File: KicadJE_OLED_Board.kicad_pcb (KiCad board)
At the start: 2 copper layers, 170.6 x 128 mm, 189 parts, among them J1 LED 1-6, J101 Out1, J102 IN1, J103 OUT1, J104 Out1, J105 IN1, J106 OUT1, J201 OLED, J202 ADC Input, J203 Out2, J204 Out1, J205 OUT1, J206 OUT2, J207 IN1, J208 IN2, J209 CV1, J210 CV2, J211 FrontLED, J212 -12V Front, J301 UART, J302 AVR-ISP-6, P1 Doepfer_Power_16pin, P101 Doepfer_Power_10pin, P201 Doepfer_Power_16pin, SW201 Rotary_Encoder_Switch, SW202 Rotary_Encoder_Switch, U101 TL072, U201 TL072, U202 TL072, U301 ATmega32A-AU, Y301 16MHz

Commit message: Update KicadJE_OLED_Board.kicad_pcb
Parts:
- C105, C106, D101, D102, R112: moved to F.Cu
- moved D105 142.4 mm to (125.6, 130.1)
- moved D106 142.4 mm to (125.6, 133.5)
- moved D104 132.4 mm to (133.0, 130.0)
- moved D101 128.5 mm to (144.0, 61.0), turned to 270 degrees
- moved D107 127.5 mm to (133.0, 134.0)
- moved D102 112.9 mm to (144.0, 69.0), turned to 270 degrees
- moved C105 105.6 mm to (154.0, 90.0), turned to 180 degrees
- moved J101 104.8 mm to (147.0, 106.0)
- moved C106 102.3 mm to (148.1, 81.5), turned to 180 degrees
- moved J104 99.0 mm to (153.0, 106.0)
- moved U101 75.2 mm to (151.0, 86.0)
- moved R112 65.6 mm to (155.0, 65.0), turned to 270 degrees
- moved TP101 53.9 mm to (143.0, 45.0)
- moved R109 34.7 mm to (168.0, 34.0)
- moved H101 31.7 mm to (151.0, 47.0)
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
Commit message: Amp/Filt
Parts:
- added J107: In1, Connector_PinSocket_2.54mm:PinSocket_1x02_P2.54mm_Vertical, B.Cu at (148.0, 98.2)
- added J108: InFlt, Connector_PinSocket_2.54mm:PinSocket_1x02_P2.54mm_Vertical, B.Cu at (152.0, 98.2)
- J104: value Out1 -> OutFlt
- J105: value IN1 -> INFLT
- J106: value OUT1 -> OUTFLT
- moved R103 111.2 mm to (148.0, 115.0)
- moved R114 106.7 mm to (148.0, 125.0)
- moved R113 72.1 mm to (101.8, 26.5)
- moved R104 71.3 mm to (107.3, 26.5)
- moved R106 70.7 mm to (112.8, 26.5)
- moved C103 60.3 mm to (102.0, 39.0)
- moved R102 60.3 mm to (108.0, 35.0)
- moved R117 49.5 mm to (118.2, 26.5)
- moved R109 48.9 mm to (136.0, 71.0)
- moved R110 48.8 mm to (123.7, 26.5)
- moved R105 47.5 mm to (129.2, 26.5)
- moved D105 31.2 mm to (151.0, 112.0), turned to 90 degrees
- moved D106 26.2 mm to (151.0, 127.0), turned to 90 degrees
- moved C104 25.0 mm to (134.6, 26.5)
- moved D104 22.2 mm to (151.0, 117.0), turned to 90 degrees
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
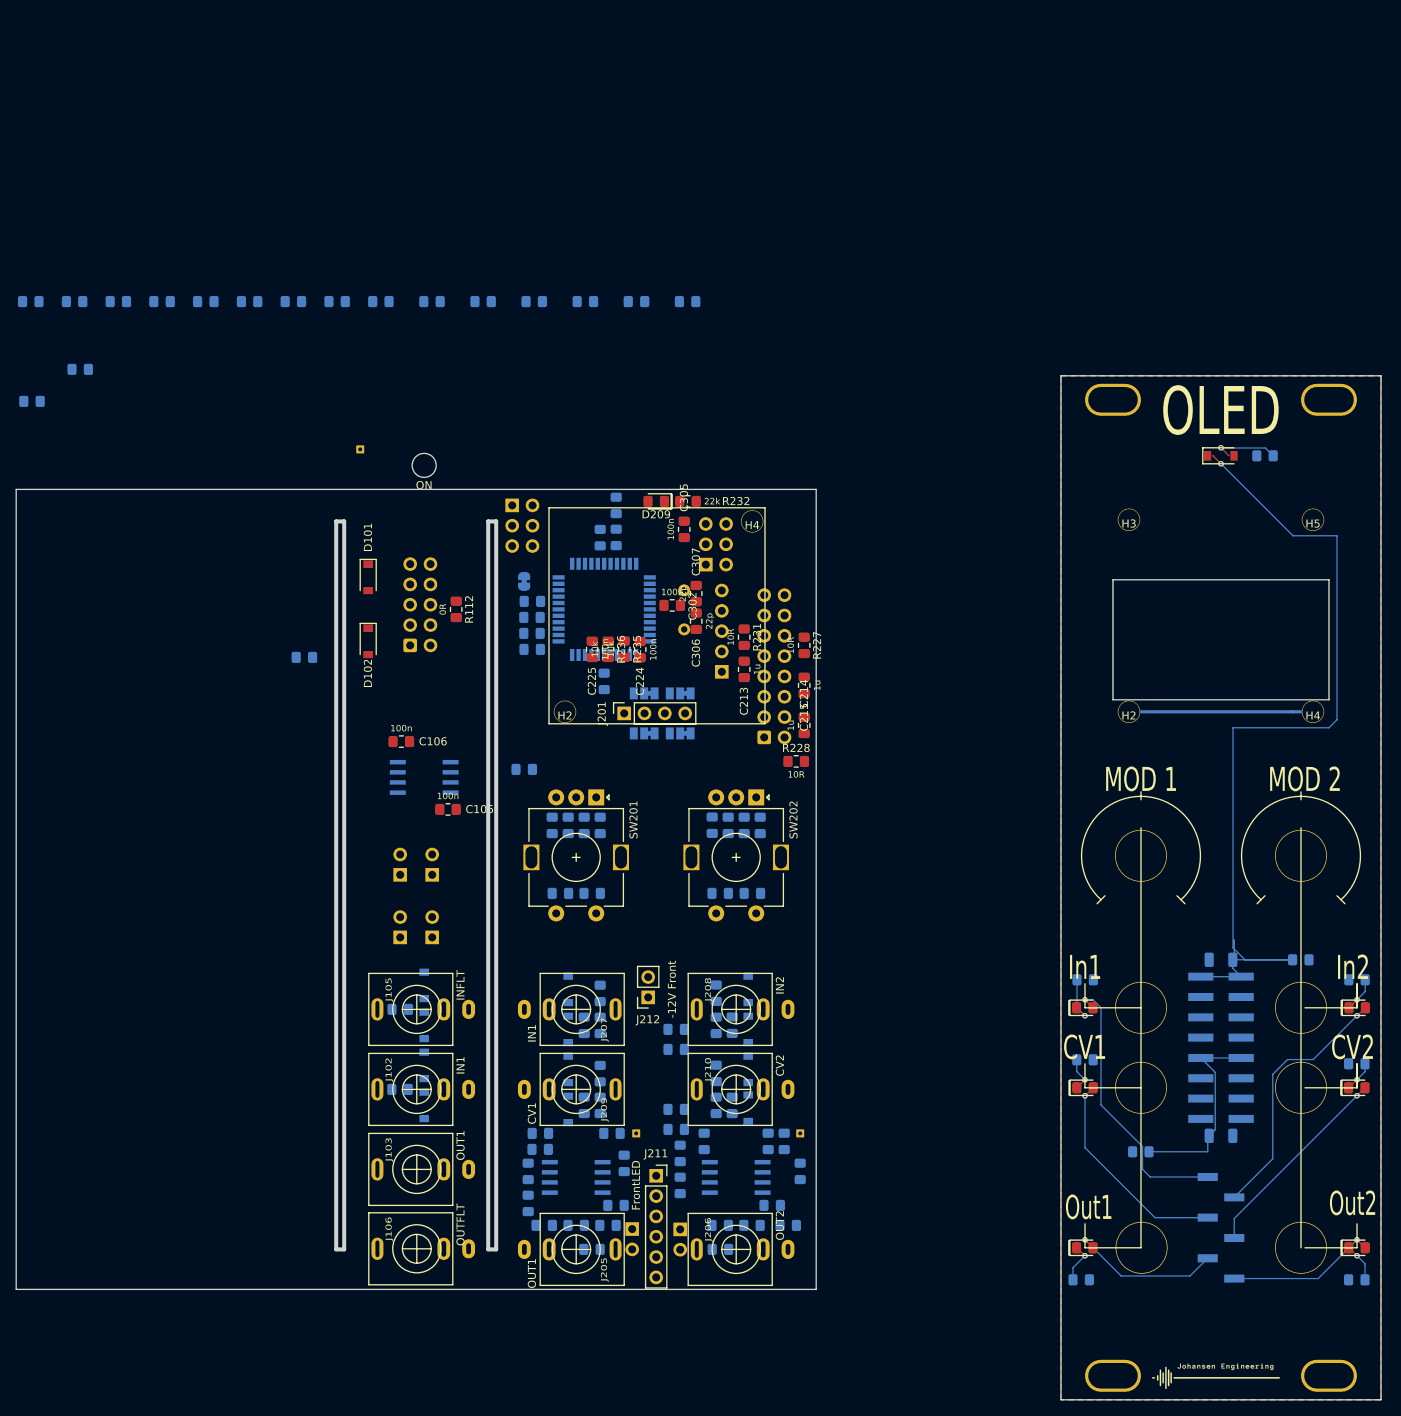
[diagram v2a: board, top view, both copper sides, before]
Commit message: move pinhdr from in jacks to input circuit
after protection resistor - so pcb may be cut above the connectors in case this is needed
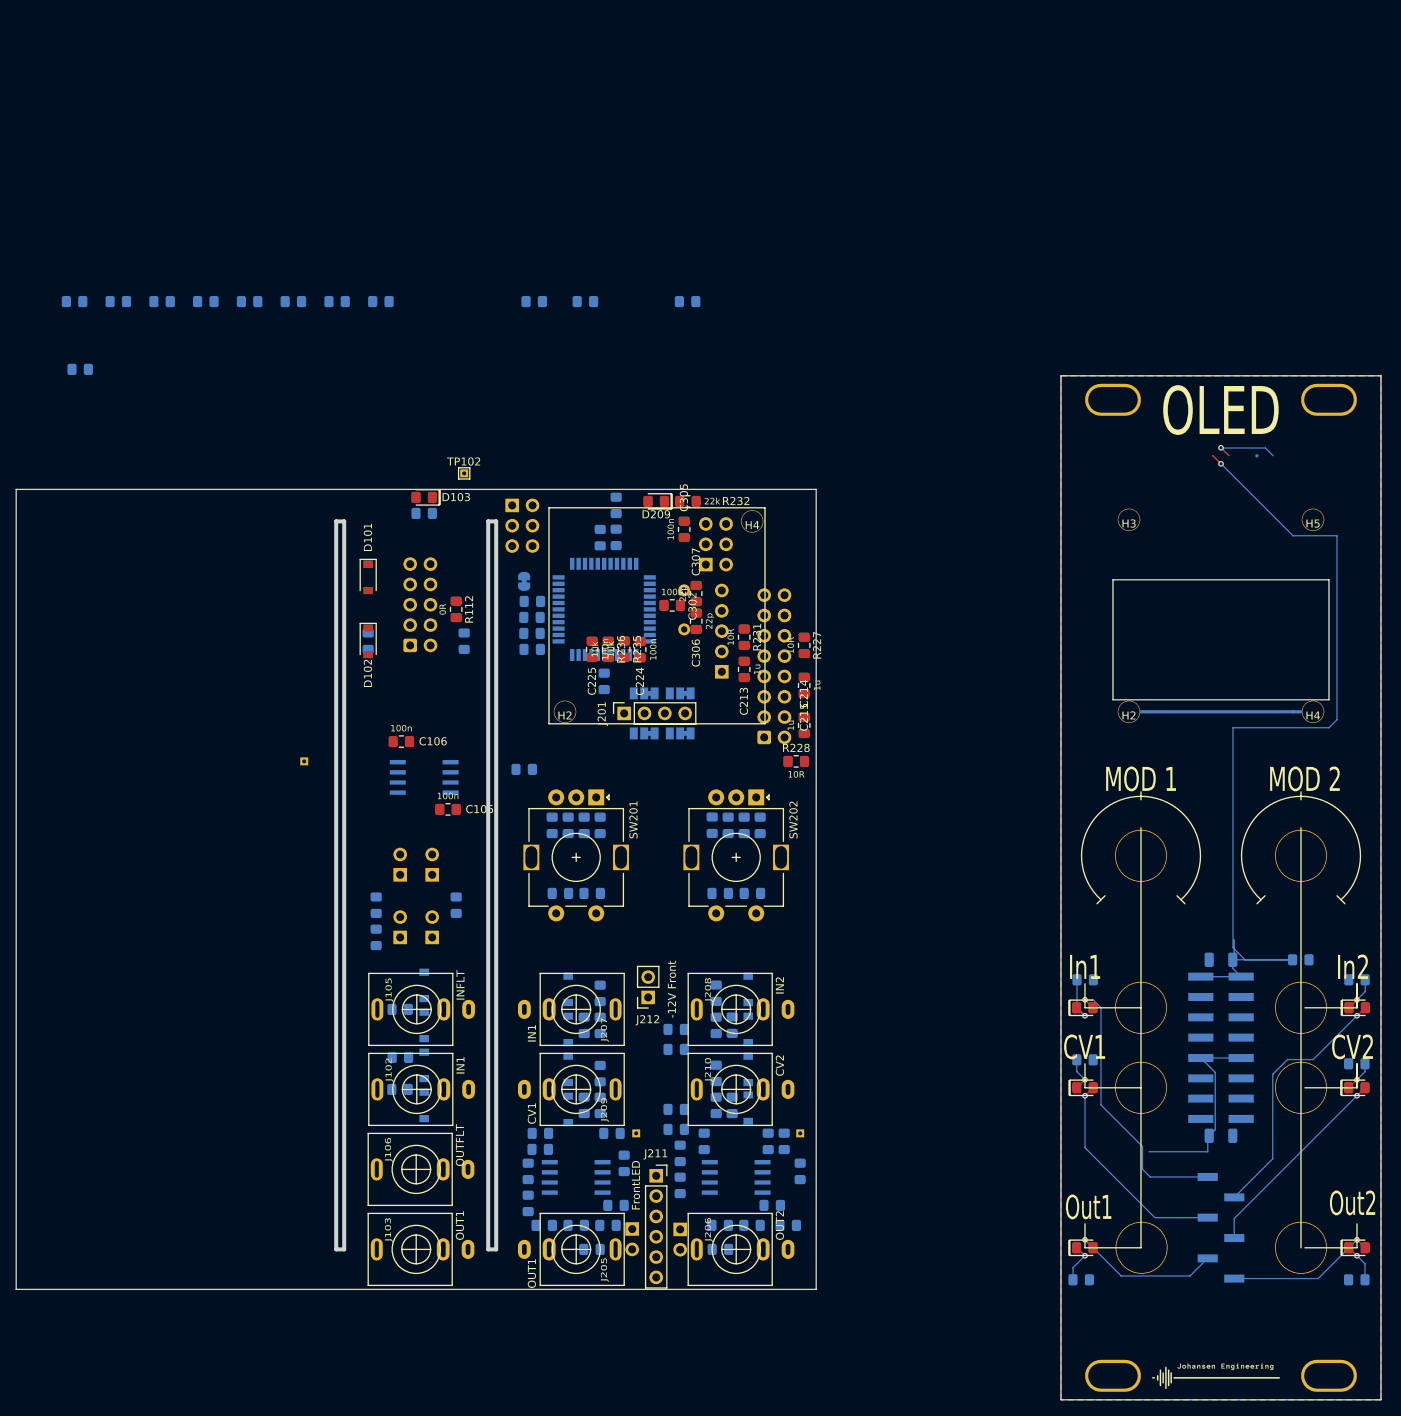
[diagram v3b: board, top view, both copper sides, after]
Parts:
- removed the C103 at (240.6, 132.8)
- removed H101: ON, AJ:LED_Hole_3mm
- added TP102: AmpOut1, TestPoint:TestPoint_THTPad_1.0x1.0mm_Drill0.5mm, F.Cu at (156.0, 48.0)
- D103: footprint AJ:D_SOD-123 -> AJ:D_0805_AJ
- moved R101 105.3 mm to (151.0, 53.0), turned to 180 degrees
- moved D103 99.7 mm to (151.0, 51.0), turned to 180 degrees
- moved R115 95.0 mm to (148.0, 121.0), turned to 180 degrees
- moved R113 86.9 mm to (145.0, 102.0), turned to 90 degrees
- moved C103 79.6 mm to (145.0, 106.0), turned to 270 degrees
- moved R118 78.7 mm to (155.0, 102.0), turned to 270 degrees
- moved R108 42.6 mm to (156.0, 69.0), turned to 270 degrees
- moved TP101 39.6 mm to (136.0, 84.0)
- moved J103 10.0 mm to (150.0, 145.0)
- moved J106 9.93 mm to (150.0, 135.0)
- moved R109 8.23 mm to (144.0, 69.0), turned to 270 degrees
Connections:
- J107 pad 2: In1_Amp -> Net-(D104-Pad2)
- J108 pad 1: GNDA -> GND
- J108 pad 2: In1_Filt -> Net-(D106-Pad2)

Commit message: placed amp/filt
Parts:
- removed the C101 at (250.6, 130.8)
- moved R102 104.2 mm to (155.0, 128.0), turned to 180 degrees
- moved R110 96.7 mm to (155.0, 118.0), turned to 180 degrees
- moved R104 77.7 mm to (144.0, 95.0), turned to 180 degrees
- moved R111 72.3 mm to (145.0, 87.5), turned to 270 degrees
- moved R117 69.2 mm to (157.5, 83.5), turned to 270 degrees
- moved C101 67.2 mm to (143.0, 87.5), turned to 270 degrees
- moved R107 64.4 mm to (151.1, 90.0)
- moved R106 61.0 mm to (143.0, 79.5), turned to 90 degrees
- moved R105 59.1 mm to (145.0, 83.5), turned to 90 degrees
- moved C104 56.9 mm to (155.5, 79.5), turned to 90 degrees
- moved C102 56.6 mm to (145.0, 79.5), turned to 90 degrees
- moved R116 54.3 mm to (157.5, 79.5), turned to 270 degrees
- moved TP102 38.5 mm to (157.5, 86.5)
- moved R115 27.2 mm to (156.0, 95.0), turned to 0 degrees
- moved R112 9.37 mm to (151.0, 73.5)
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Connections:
- C105 pad 2: GND -> GNDA
- C106 pad 1: GND -> GNDA
